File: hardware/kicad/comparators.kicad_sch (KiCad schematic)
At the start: 16 parts, among them U1001 MCP6562-E/SN, U1002 MCP6561T-E/OT

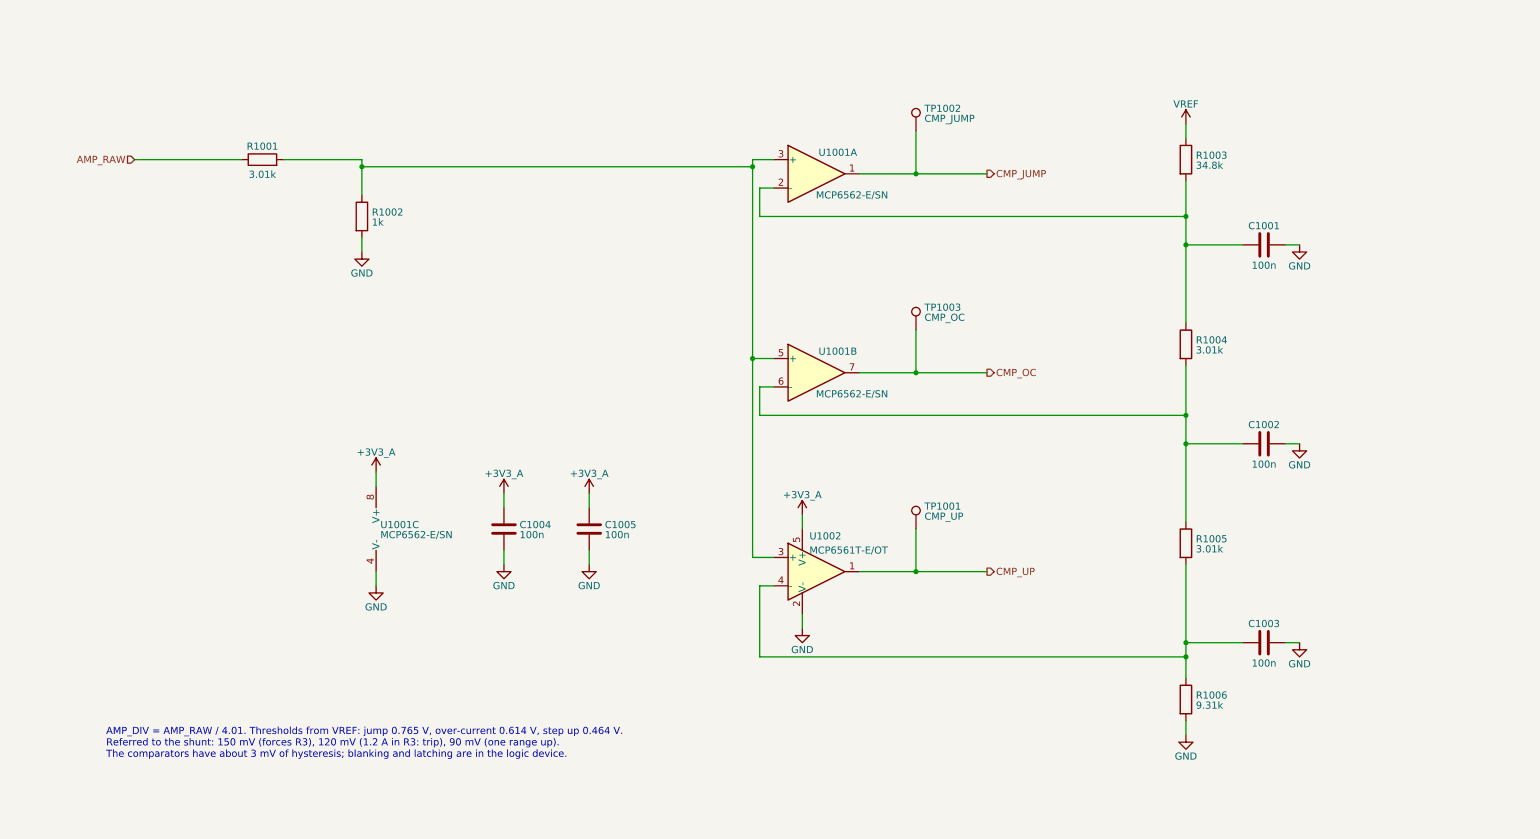
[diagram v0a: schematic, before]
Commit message: feat(hardware)!: draw draft A1 of the schematic around a Pico 2
A Raspberry Pi Pico 2 on two 1x20 sockets replaces the ESP32-S3
development board, the programmable logic device and the buffer
between the two boards (D-39 to D-43 of the specification). The former
interface and range logic sheets become two new ones:

- Controller: the Pico 2, the diodes that join its USB supply and the
  5 V rail of the carrier, resistor arrays in the SPI and acquisition
  lines, a reset button and a console header.
- Side Data: two shift registers that take the range, the status
  signals and the eight logic inputs with every sample.

The DUT connects through a 1x4 pin header and a lever terminal block
in parallel, both GND, VIN, VOUT, GND, and the logic port is a 1x10
header with VCC, GND, D7 to D0: the pin order of the PPK2 (D-44). A
solder jumper selects the supply of the DUT side of the level
translator. A transistor at the driver of the ampere switch holds it
open while VIN is above 5.5 V.

Reference designators are numbered as the annotation tool of KiCad
does by default (D-45). The numbering touches every sheet, so these
changes come in one commit. The symbol and the socket footprint of
the ESP32-S3 board leave the project library; the Pico 2 uses the
symbol and the footprint of the KiCad library.

The electrical rules check reports no errors and no warnings. The
parts stay candidates, and no program for the PIO blocks exists yet.

BREAKING CHANGE: the pins of the controller follow the new pin map of
section 5 of the specification.
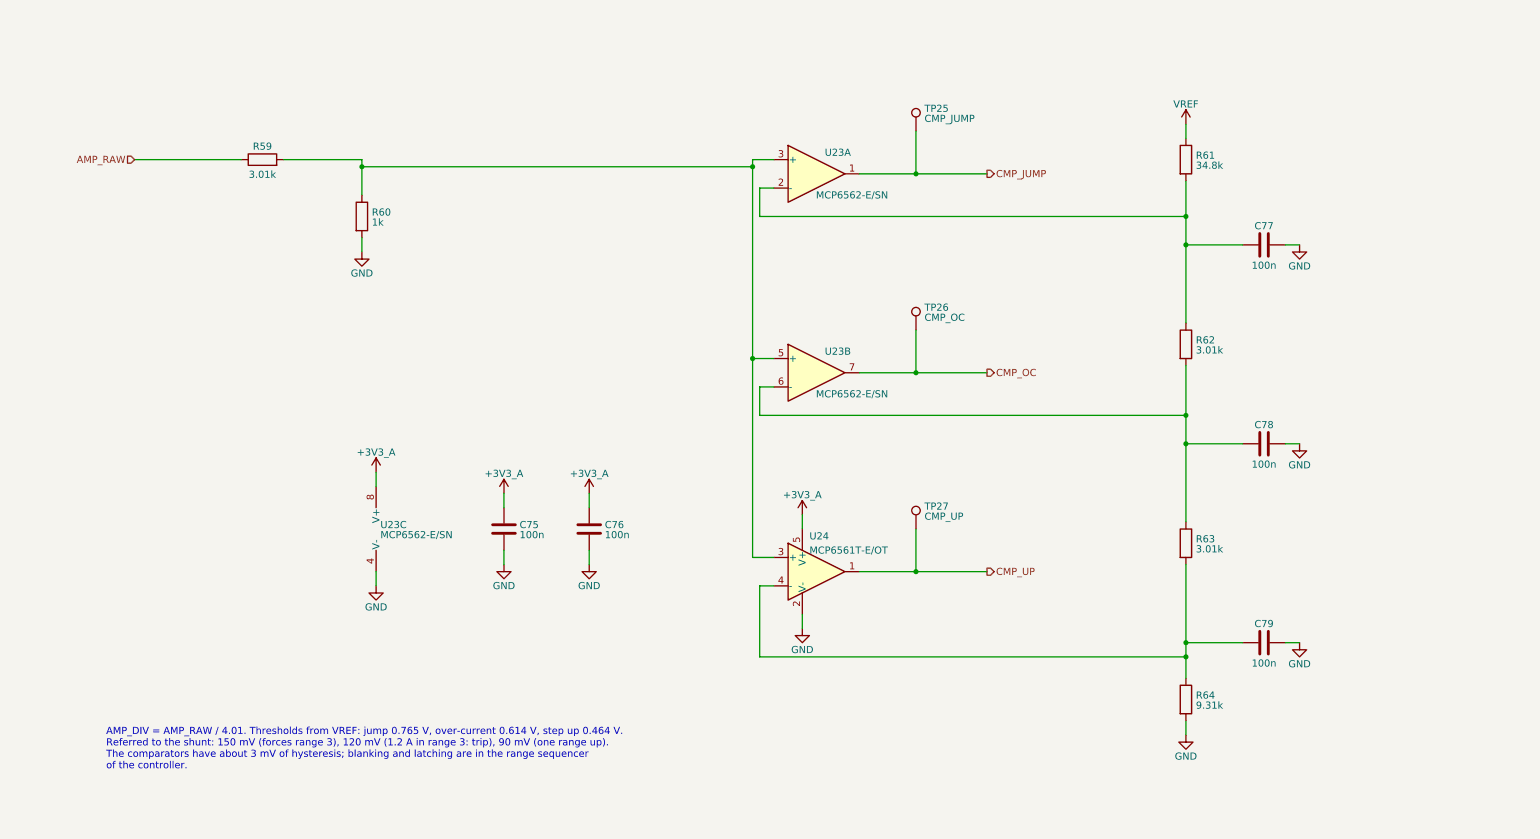
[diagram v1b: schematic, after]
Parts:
- renumbered C1004 to C75, C1005 to C76, C1001 to C77, C1002 to C78, C1003 to C79, R1001 to R59, R1002 to R60, R1003 to R61, R1004 to R62, R1005 to R63, R1006 to R64, TP1002 to TP25, TP1003 to TP26, TP1001 to TP27, U1001 to U23, U1002 to U24
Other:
- note added: "AMP_DIV = AMP_RAW / 4.01. Thresholds from VREF: jump 0.765 V, over-current 0.614 V, step up 0.464 V. Referred to the shunt: 150 mV (forces range 3), 120 mV (1.2 A in range 3: trip), 90 mV (one range up). The comparators have about 3 mV of hysteresis; blanking and latching are in the range sequencer of the controller."
- note removed: "AMP_DIV = AMP_RAW / 4.01. Thresholds from VREF: jump 0.765 V, over-current 0.614 V, step up 0.464 V. Referred to the shunt: 150 mV (forces R3), 120 mV (1.2 A in R3: trip), 90 mV (one range up). The comparators have about 3 mV of hysteresis; blanking and latching are in the logic device."
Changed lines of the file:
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@@
 		(title "Range and Over-current Comparators")
 		(date "2026-10-08")
-		(rev "A0 (draft)")
-		(comment 1 "Step up at 90 mV, over-current at 120 mV, jump to R3 at 150 mV across the shunt")
+		(rev "A1 (draft)")
+		(comment 1 "Step up at 90 mV, over-current at 120 mV, jump to range 3 at 150 mV across the shunt")
 	)
-	(text "AMP_DIV = AMP_RAW / 4.01. Thresholds from VREF: jump 0.765 V, over-current 0.614 V, step up 0.464 V.\nReferred to the shunt: 150 mV (forces R3), 120 mV (1.2 A in R3: trip), 90 mV (one range up).\nThe comparators have about 3 mV of hysteresis; blanking and latching are in the logic device."
+	(text "AMP_DIV = AMP_RAW / 4.01. Thresholds from VREF: jump 0.765 V, over-current 0.614 V, step up 0.464 V.\nReferred to the shunt: 150 mV (forces range 3), 120 mV (1.2 A in range 3: trip), 90 mV (one range up).\nThe comparators have about 3 mV of hysteresis; blanking and latching are in the range sequencer\nof the controller."
 		(exclude_from_sim no)
 		(at 30.48 152.4 0)
@@
 		(in_pos_files yes)
 		(dnp no)
-		(property "Reference" "U1001"
+		(property "Reference" "U23"
 			(at 161.29 49.53 0)
 			(show_name no)
@@
 			(project "power-profiler-carrier"
 				(path "/f565bb5d-729e-50de-bc50-2ad3654b1f99/d5ed0f1b-5e9e-5f6c-ad1b-4821c01ea280"
-					(reference "U1001")
+					(reference "U23")
 					(unit 1)
 				)
@@
 		(in_pos_files yes)
 		(dnp no)
-		(property "Reference" "R1002"
+		(property "Reference" "R60"
 			(at 77.976 60.21 0)
 			(show_name no)
@@
 			(project "power-profiler-carrier"
 				(path "/f565bb5d-729e-50de-bc50-2ad3654b1f99/d5ed0f1b-5e9e-5f6c-ad1b-4821c01ea280"
-					(reference "R1002")
+					(reference "R60")
 					(unit 1)
 				)
@@
 		(in_pos_files yes)
 		(dnp no)
-		(property "Reference" "C1005"
+		(property "Reference" "C76"
 			(at 119.632 116.09 0)
 			(show_name no)
@@
 			(project "power-profiler-carrier"
 				(path "/f565bb5d-729e-50de-bc50-2ad3654b1f99/d5ed0f1b-5e9e-5f6c-ad1b-4821c01ea280"
-					(reference "C1005")
+					(reference "C76")
 					(unit 1)
 				)
@@
 		(in_pos_files yes)
 		(dnp no)
-		(property "Reference" "R1001"
+		(property "Reference" "R59"
 			(at 58.42 48.434 90)
 			(show_name no)
@@
 			(project "power-profiler-carrier"
 				(path "/f565bb5d-729e-50de-bc50-2ad3654b1f99/d5ed0f1b-5e9e-5f6c-ad1b-4821c01ea280"
-					(reference "R1001")
+					(reference "R59")
 					(unit 1)
 				)
@@
 		(in_pos_files yes)
 		(dnp no)
-		(property "Reference" "R1003"
+		(property "Reference" "R61"
 			(at 225.296 50.05 0)
 			(show_name no)
@@
 			(project "power-profiler-carrier"
 				(path "/f565bb5d-729e-50de-bc50-2ad3654b1f99/d5ed0f1b-5e9e-5f6c-ad1b-4821c01ea280"
-					(reference "R1003")
+					(reference "R61")
 					(unit 1)
 				)
@@
 		(in_pos_files yes)
 		(dnp no)
-		(property "Reference" "C1004"
+		(property "Reference" "C75"
 			(at 104.392 116.09 0)
 			(show_name no)
@@
 			(project "power-profiler-carrier"
 				(path "/f565bb5d-729e-50de-bc50-2ad3654b1f99/d5ed0f1b-5e9e-5f6c-ad1b-4821c01ea280"
-					(reference "C1004")
+					(reference "C75")
 					(unit 1)
 				)
@@
 		(in_pos_files yes)
 		(dnp no)
-		(property "Reference" "C1002"
+		(property "Reference" "C78"
 			(at 237.49 98.218 90)
 			(show_name no)
@@
 			(project "power-profiler-carrier"
 				(path "/f565bb5d-729e-50de-bc50-2ad3654b1f99/d5ed0f1b-5e9e-5f6c-ad1b-4821c01ea280"
-					(reference "C1002")
+					(reference "C78")
 					(unit 1)
 				)
@@
 		(in_pos_files yes)
 		(dnp no)
-		(property "Reference" "R1006"
+		(property "Reference" "R64"
 			(at 225.296 146.57 0)
 			(show_name no)
@@
 			(project "power-profiler-carrier"
 				(path "/f565bb5d-729e-50de-bc50-2ad3654b1f99/d5ed0f1b-5e9e-5f6c-ad1b-4821c01ea280"
-					(reference "R1006")
+					(reference "R64")
 					(unit 1)
 				)
@@
 		(in_pos_files yes)
 		(dnp no)
-		(property "Reference" "U1001"
+		(property "Reference" "U23"
 			(at 79.5 116.09 0)
 			(show_name no)
@@
 			(project "power-profiler-carrier"
 				(path "/f565bb5d-729e-50de-bc50-2ad3654b1f99/d5ed0f1b-5e9e-5f6c-ad1b-4821c01ea280"
-					(reference "U1001")
+					(reference "U23")
 					(unit 3)
 				)
@@
 		(in_pos_files yes)
 		(dnp no)
-		(property "Reference" "R1004"
+		(property "Reference" "R62"
 			(at 225.296 83.07 0)
 			(show_name no)
@@
 			(project "power-profiler-carrier"
 				(path "/f565bb5d-729e-50de-bc50-2ad3654b1f99/d5ed0f1b-5e9e-5f6c-ad1b-4821c01ea280"
-					(reference "R1004")
+					(reference "R62")
 					(unit 1)
 				)
@@
 		(in_pos_files yes)
 		(dnp no)
-		(property "Reference" "TP1001"
+		(property "Reference" "TP27"
 			(at 176.782 112.788 0)
 			(show_name no)
@@
 			(project "power-profiler-carrier"
 				(path "/f565bb5d-729e-50de-bc50-2ad3654b1f99/d5ed0f1b-5e9e-5f6c-ad1b-4821c01ea280"
-					(reference "TP1001")
+					(reference "TP27")
 					(unit 1)
 				)
@@
 		(in_pos_files yes)
 		(dnp no)
-		(property "Reference" "C1001"
+		(property "Reference" "C77"
 			(at 237.49 62.658 90)
 			(show_name no)
@@
 			(project "power-profiler-carrier"
 				(path "/f565bb5d-729e-50de-bc50-2ad3654b1f99/d5ed0f1b-5e9e-5f6c-ad1b-4821c01ea280"
-					(reference "C1001")
+					(reference "C77")
 					(unit 1)
 				)
@@
 		(in_pos_files yes)
 		(dnp no)
-		(property "Reference" "U1001"
+		(property "Reference" "U23"
 			(at 161.29 85.09 0)
 			(show_name no)
@@
 			(project "power-profiler-carrier"
 				(path "/f565bb5d-729e-50de-bc50-2ad3654b1f99/d5ed0f1b-5e9e-5f6c-ad1b-4821c01ea280"
-					(reference "U1001")
+					(reference "U23")
 					(unit 2)
 				)
@@
 		(in_pos_files yes)
 		(dnp no)
-		(property "Reference" "TP1003"
+		(property "Reference" "TP26"
 			(at 176.782 77.228 0)
 			(show_name no)
@@
 			(project "power-profiler-carrier"
 				(path "/f565bb5d-729e-50de-bc50-2ad3654b1f99/d5ed0f1b-5e9e-5f6c-ad1b-4821c01ea280"
-					(reference "TP1003")
+					(reference "TP26")
 					(unit 1)
 				)
@@
 		(in_pos_files yes)
 		(dnp no)
-		(property "Reference" "TP1002"
+		(property "Reference" "TP25"
 			(at 176.782 41.668 0)
 			(show_name no)
@@
 			(project "power-profiler-carrier"
 				(path "/f565bb5d-729e-50de-bc50-2ad3654b1f99/d5ed0f1b-5e9e-5f6c-ad1b-4821c01ea280"
-					(reference "TP1002")
+					(reference "TP25")
 					(unit 1)
 				)
@@
 		(in_pos_files yes)
 		(dnp no)
-		(property "Reference" "U1002"
+		(property "Reference" "U24"
 			(at 156.21 118.11 0)
 			(show_name no)
@@
 			(project "power-profiler-carrier"
 				(path "/f565bb5d-729e-50de-bc50-2ad3654b1f99/d5ed0f1b-5e9e-5f6c-ad1b-4821c01ea280"
-					(reference "U1002")
+					(reference "U24")
 					(unit 1)
 				)
@@
 		(in_pos_files yes)
 		(dnp no)
-		(property "Reference" "C1003"
+		(property "Reference" "C79"
 			(at 237.49 133.778 90)
 			(show_name no)
@@
 			(project "power-profiler-carrier"
 				(path "/f565bb5d-729e-50de-bc50-2ad3654b1f99/d5ed0f1b-5e9e-5f6c-ad1b-4821c01ea280"
-					(reference "C1003")
+					(reference "C79")
 					(unit 1)
 				)
@@
 		(in_pos_files yes)
 		(dnp no)
-		(property "Reference" "R1005"
+		(property "Reference" "R63"
 			(at 225.296 118.63 0)
 			(show_name no)
@@
 			(project "power-profiler-carrier"
 				(path "/f565bb5d-729e-50de-bc50-2ad3654b1f99/d5ed0f1b-5e9e-5f6c-ad1b-4821c01ea280"
-					(reference "R1005")
+					(reference "R63")
 					(unit 1)
 				)

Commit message: feat(hardware): draw draft A2 of the schematic
428 parts on 15 A4 pages, 14 sheets below the root sheet (D-83). Two
sheets are new: Logic Supplies, with the supervisor of the 5 V rail and
the two 3.3 V regulators, and Rail Monitor, with the comparators behind
PWR_GOOD.

The drawings follow the specification of draft A2: a current limiter
on each supply input and a priority multiplexer, a pre-regulator that
tracks the output of the linear regulator, a VIN path that withstands
-20 V to +20 V with its switch open, two diode-connected MOSFETs as
ladder clamp, thin-film and four-terminal shunts, ESD arrays at the CC
pins and at the VCC pin of the logic port. The reference designators
are numbered as KiCad numbers them (D-45), so they are not those of
draft A1.

The project library gains the symbol of the input multiplexer and two
footprints: the lever terminal block with pads of 1.9 mm x 2.3 mm and
the controller module without its antenna keep-out (D-85).

The electrical rules check reports no errors and no warnings. The
parts are candidates, and nothing is built or measured.
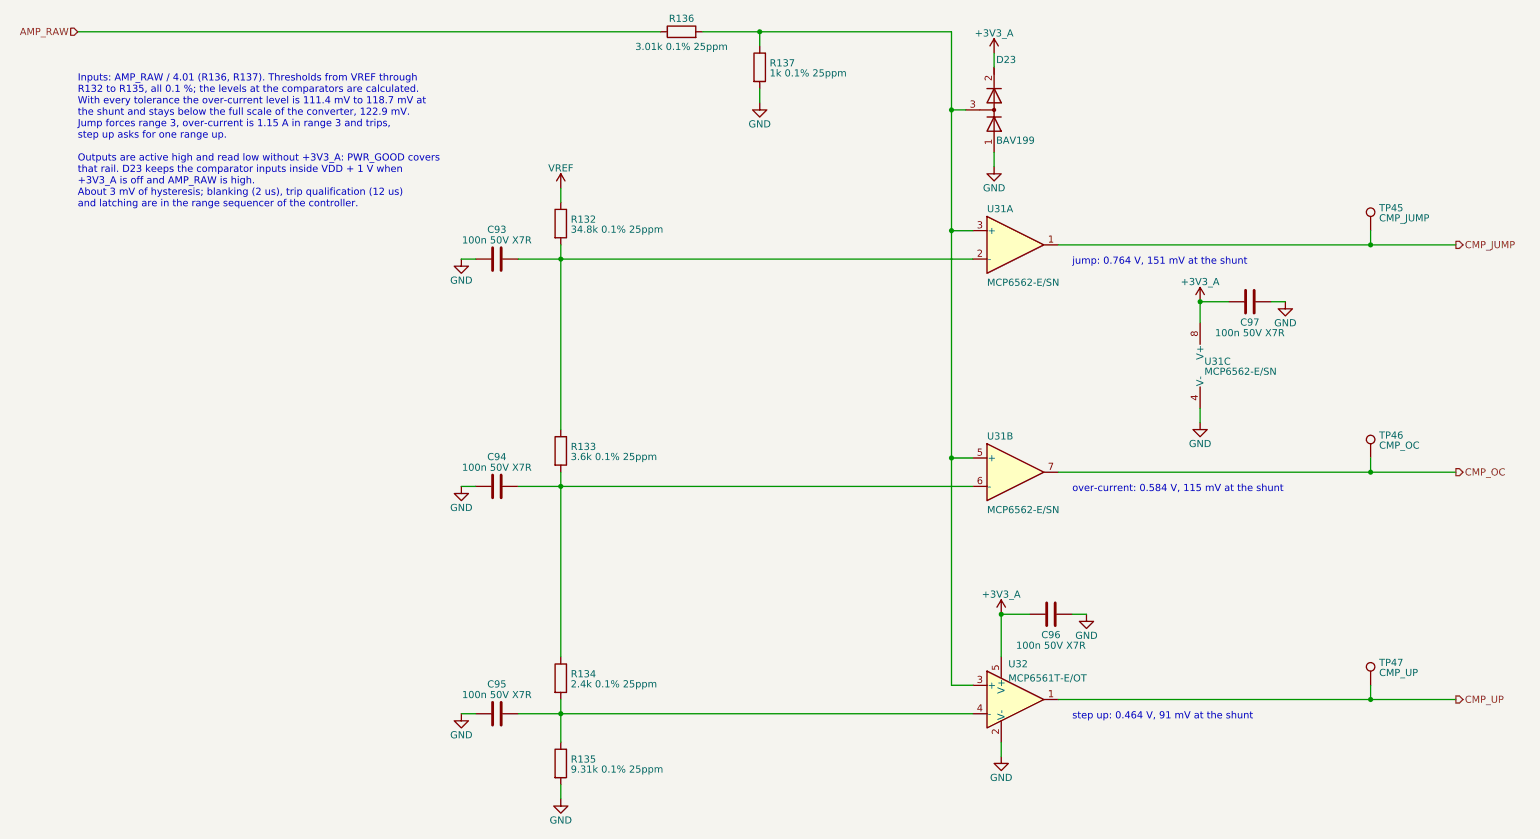
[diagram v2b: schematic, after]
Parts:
- added D23: BAV199, Package_TO_SOT_SMD:SOT-23, symbol Device:D_Dual_Series_AKC
- C93: renamed from C77; value 100n -> 100n 50V X7R; MPN (none) -> C0603C104K5RACTU; Manufacturer (none) -> KEMET
- C94: renamed from C78; value 100n -> 100n 50V X7R; MPN (none) -> C0603C104K5RACTU; Manufacturer (none) -> KEMET
- C95: renamed from C79; value 100n -> 100n 50V X7R; MPN (none) -> C0603C104K5RACTU; Manufacturer (none) -> KEMET
- C96: renamed from C76; value 100n -> 100n 50V X7R; MPN (none) -> C0603C104K5RACTU; Manufacturer (none) -> KEMET
- C97: renamed from C75; value 100n -> 100n 50V X7R; MPN (none) -> C0603C104K5RACTU; Manufacturer (none) -> KEMET
- R132: renamed from R61; value 34.8k -> 34.8k 0.1% 25ppm; MPN (none) -> TNPW060334K8BEEA; Manufacturer (none) -> Vishay
- R133: renamed from R62; value 3.01k -> 3.6k 0.1% 25ppm; MPN (none) -> TNPW06033K60BEEA; Manufacturer (none) -> Vishay
- R134: renamed from R63; value 3.01k -> 2.4k 0.1% 25ppm; MPN (none) -> TNPW06032K40BEEA; Manufacturer (none) -> Vishay
- R135: renamed from R64; value 9.31k -> 9.31k 0.1% 25ppm; MPN (none) -> TNPW06039K31BEEA; Manufacturer (none) -> Vishay
- R136: renamed from R59; value 3.01k -> 3.01k 0.1% 25ppm; MPN (none) -> ERA-3AEB3011V; Manufacturer (none) -> Panasonic
- R137: renamed from R60; value 1k -> 1k 0.1% 25ppm; MPN (none) -> TNPW06031K00BEEA; Manufacturer (none) -> Vishay
- TP45: renamed from TP25; now left out of the parts list
- TP46: renamed from TP26; now left out of the parts list
- TP47: renamed from TP27; now left out of the parts list
- U31: renamed from U23; MPN (none) -> MCP6562-E/SN; Manufacturer (none) -> Microchip
- U32: renamed from U24; MPN (none) -> MCP6561T-E/OT; Manufacturer (none) -> Microchip
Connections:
- net +3V3_A: now also D23.2 (K)
- net GND: now also D23.1 (A)
- net at R136.2, R137.1, U31.3 (+)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: now also D23.3 (common)
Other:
- note added: "Inputs: AMP_RAW / 4.01 (R136, R137). Thresholds from VREF through R132 to R135, all 0.1 %; the levels at the comparators are calculated. With every tolerance the over-current level is 111.4 mV to 118.7 mV at the shunt and stays below the full scale of the converter, 122.9 mV. Jump forces range 3, over-current is 1.15 A in range 3 and trips, step up asks for one range up. Outputs are active high a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"
- note added: "jump: 0.764 V, 151 mV at the shunt"
- note added: "over-current: 0.584 V, 115 mV at the shunt"
- note added: "step up: 0.464 V, 91 mV at the shunt"
- note removed: "AMP_DIV = AMP_RAW / 4.01. Thresholds from VREF: jump 0.765 V, over-current 0.614 V, step up 0.464 V. Referred to the shunt: 150 mV (forces range 3), 120 mV (1.2 A in range 3: trip), 90 mV (one range up). The comparators have about 3 mV of hysteresis; blanking and latching are in the range sequencer of the controller."
- moved on the sheet: C93, C94, C95, C96, C97, R132, R133, R134, R135, R136, R137, TP45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
